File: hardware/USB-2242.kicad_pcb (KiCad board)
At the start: 2 copper layers, 22 x 42 mm, 19 parts, among them J1 Bus_M.2_Socket_B, U1 TPS613222ADBV

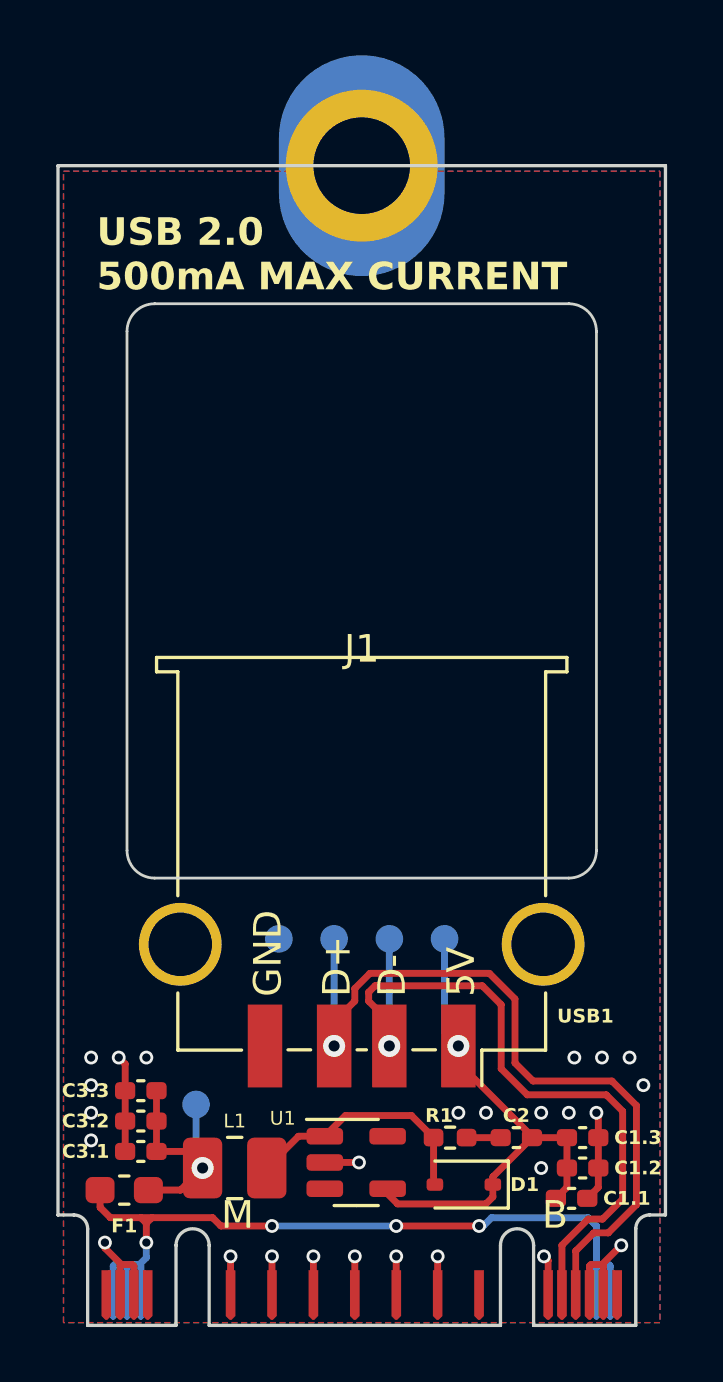
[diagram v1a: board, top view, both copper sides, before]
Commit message: Replace USB port and make various minor changes to project
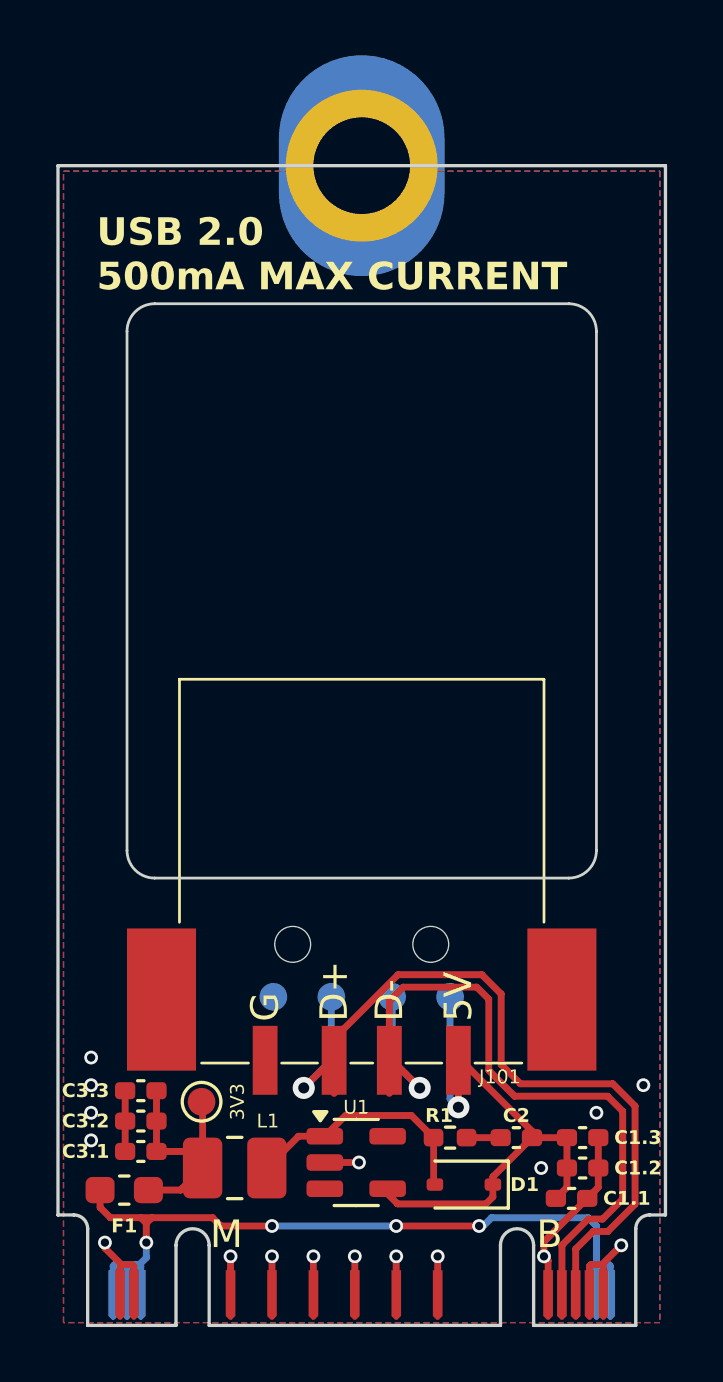
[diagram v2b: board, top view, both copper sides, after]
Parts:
- removed USB1: USB, Connector_USB:USB_A_TE_292303-7_Horizontal
- added J101: USB_A, Adam-Tech:USB-A-S-RA-TSMT, F.Cu at (138.6, 107.4)
- J1: value Bus_M.2_Socket_B -> Bus_M.2_Socket_B+M_USB_Only
- TP2: moved to F.Cu
- moved TP3 2.11 mm to (141.8, 109.3)
- moved TP1 2.11 mm to (135.4, 109.3)
- moved TP4 2.10 mm to (137.5, 109.3)
- moved TP5 2.10 mm to (139.7, 109.3)
- moved TP2 0.22 mm to (132.8, 113.1), turned to 0 degrees
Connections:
- net +5V renamed VBUS
- net /BOOST IN renamed Net-(D1-A)
- net /SNUBBER RC renamed Net-(C2-Pad1)
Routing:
- net VBUS: track 19.1 -> 21.3 mm
- net /USBD+: track 29.0 -> 29.9 mm
- net GND: track 25.2 -> 25.7 mm, vias 26 -> 17
- net /3V3 PROT: track 8.81 -> 8.83 mm, vias 1 -> 0
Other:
- board text added: "${PROJECTNAME} REV.${REVISION} ${COMPANY} ${ISSUE_DATE}"
- board text added: "G"
- board text removed: "${TITLE} Rev.${REVISION} | ${ISSUE_DATE} ${COMMENT1}"
- board text removed: "GND"

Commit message: Update clearances for copper to board edge
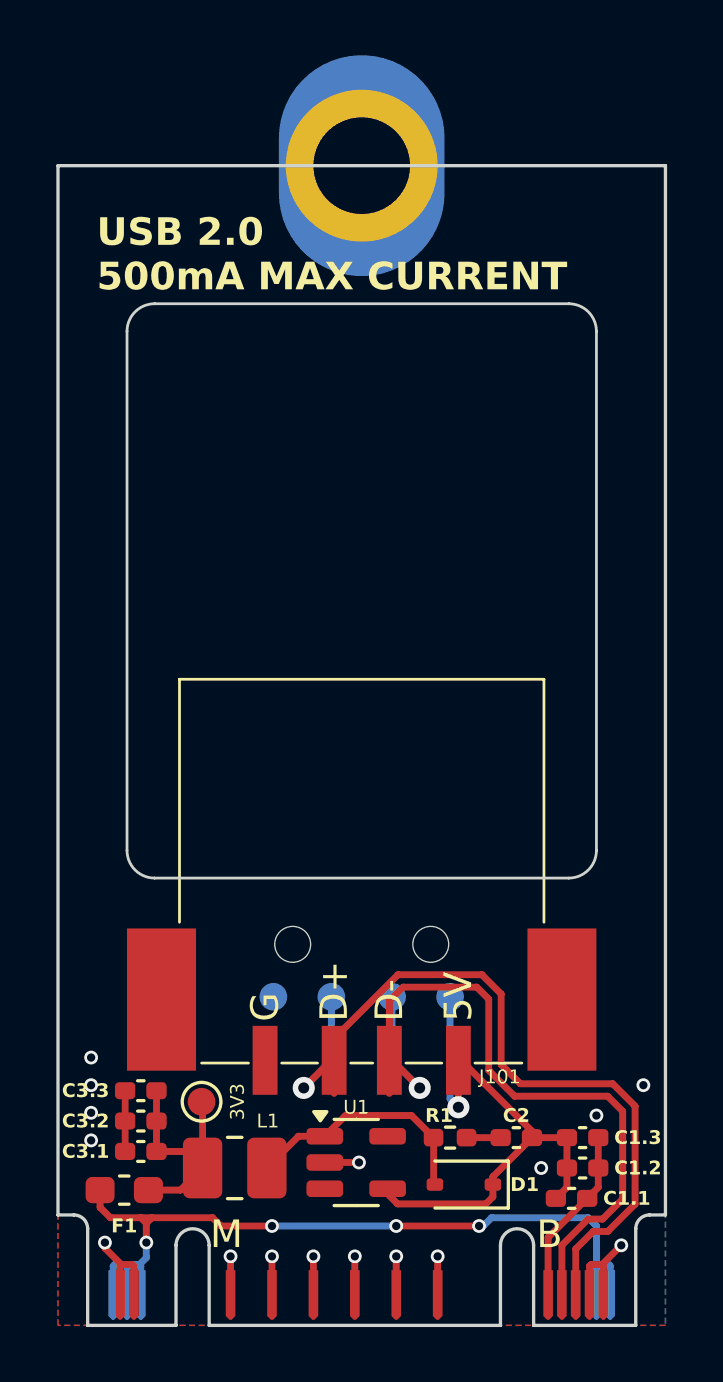
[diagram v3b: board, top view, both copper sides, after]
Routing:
- net GND: track 25.7 -> 25.6 mm, vias 17 -> 16
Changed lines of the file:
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@@
 	(title_block
 		(title "USB 2242")
-		(date "2024-08-31")
-		(rev "03A")
+		(date "2024-09-02")
+		(rev "03B")
 		(company "Embedded Shark, LLC")
 		(comment 1 "Ben Owen")
@@
 		)
 		(property "Footprint" "TestPoint:TestPoint_Pad_D1.0mm"
-			(at 0 0 360)
+			(at 0 0 0)
 			(layer "B.Fab")
 			(hide yes)
@@
 		)
 		(property "Datasheet" ""
-			(at 0 0 360)
+			(at 0 0 0)
 			(layer "B.Fab")
 			(hide yes)
@@
 		)
 		(property "Description" ""
-			(at 0 0 360)
+			(at 0 0 0)
 			(layer "B.Fab")
 			(hide yes)
@@
 	)
 	(segment
-		(start 145.2 118.1675)
-		(end 145.2 118.7)
+		(start 146.7675 116.6)
+		(end 145.35 118.0175)
 		(width 0.25)
 		(layer "F.Cu")
@@
 	)
 	(segment
-		(start 145.35 118.85)
-		(end 145.2 118.7)
-		(width 0.25)
-		(layer "F.Cu")
-		(net 1)
-	)
-	(segment
 		(start 147.3 119)
 		(end 146.9 119)
@@
 	)
 	(segment
-		(start 146.7675 116.6)
-		(end 145.2 118.1675)
-		(width 0.25)
-		(layer "F.Cu")
-		(net 1)
-	)
-	(segment
 		(start 147.1675 114.4)
 		(end 147.1675 115.5)
@@
 	)
 	(segment
-		(start 145.35 120.1)
-		(end 145.35 118.85)
-		(width 0.25)
-		(layer "F.Cu")
-		(net 1)
-	)
-	(segment
 		(start 133.85 120.1)
 		(end 133.85 118.7)
@@
 	)
 	(segment
+		(start 145.35 118.0175)
+		(end 145.35 120.1)
+		(width 0.25)
+		(layer "F.Cu")
+		(net 1)
+	)
+	(segment
 		(start 139.85 118.7)
 		(end 139.85 120.1)
@@
 	)
 	(via
-		(at 147.1 113.5)
+		(at 147.1 113.6)
 		(size 0.5)
 		(drill 0.3)
@@
 	)
 	(via
-		(at 145.2 118.7)
-		(size 0.5)
-		(drill 0.3)
-		(layers "F.Cu" "B.Cu")
-		(net 1)
-	)
-	(via
 		(at 135.35 118.7)
 		(size 0.5)
@@
 		(polygon
 			(pts
-				(xy 149.4 121.1) (xy 127.8 121.1) (xy 127.8 79.4) (xy 149.4 79.4)
+				(xy 149.6 121.2) (xy 127.6 121.2) (xy 127.6 79.2) (xy 149.6 79.2)
 			)
 		)

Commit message: Clean up silkscreen
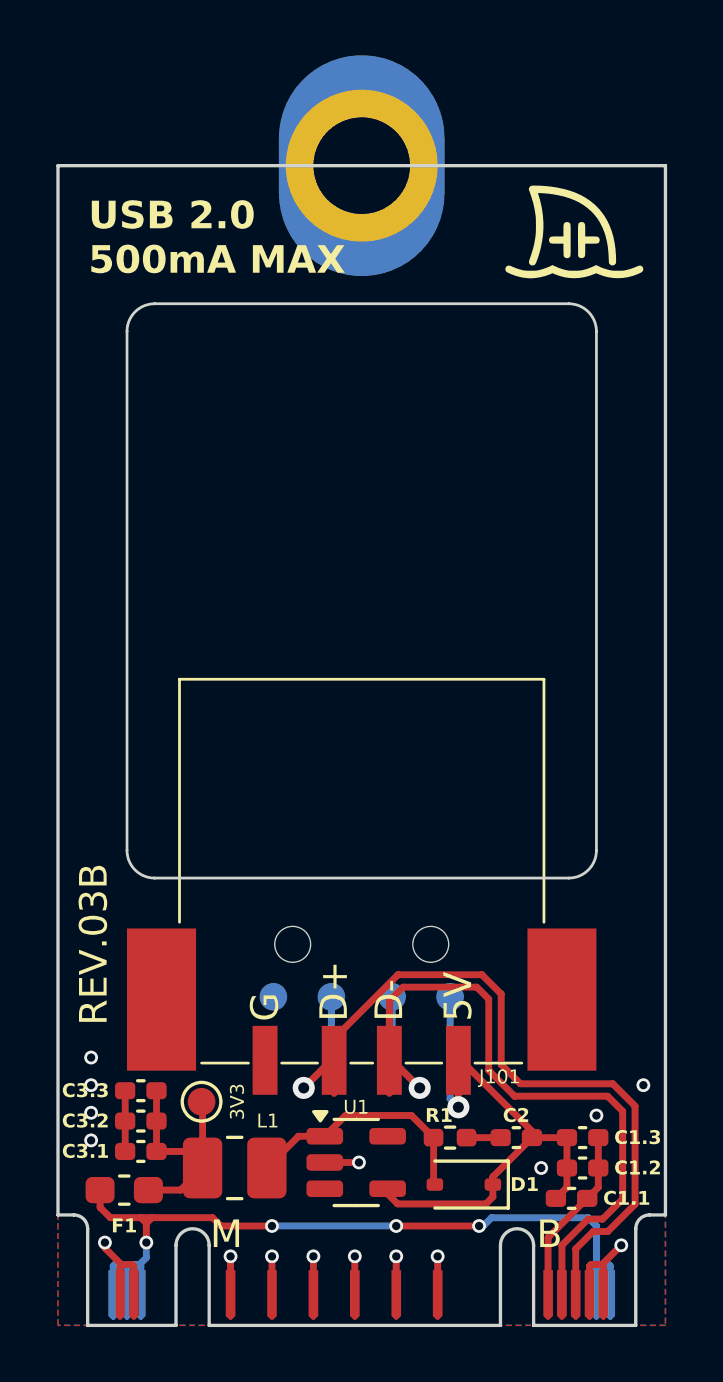
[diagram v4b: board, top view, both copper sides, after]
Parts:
- added G***: LOGO, Logos:Embedded-Shark-Logo-Inverted-5mm, F.Cu at (146.3, 81.5)
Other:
- board text added: "REV.${REVISION}"
- board text added: "USB 2.0 500mA MAX"
- board text removed: "${PROJECTNAME} REV.${REVISION} ${COMPANY} ${ISSUE_DATE}"
- board text removed: "USB 2.0 500mA MAX CURRENT"
